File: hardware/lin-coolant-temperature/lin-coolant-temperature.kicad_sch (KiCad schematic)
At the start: 25 parts, among them J1 UPDI, J2 I2C LCD, J3 Screw_Terminal_01x03, Q1 2N7002, Q2 2N7002, U1 TJA1021T, U2 ATtiny824-X, U3 PCA9536DP

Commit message: Add firmware for lin-coolant-temperature, cleanup layout
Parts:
- added D1: LED, LED_SMD:LED_0805_2012Metric_Pad1.15x1.40mm_HandSolder, symbol Device:LED
- added R5: 330, Resistor_SMD:R_0805_2012Metric_Pad1.20x1.40mm_HandSolder, symbol Device:R
- renumbered D1 to D2, R9 to R10, R5 to R6, R6 to R7, R7 to R8, R8 to R9
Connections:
- net GND: now also D1.1 (K)
- net at U2.5 (PA7): now also R5.1
- new net: D1.2 (A), R5.2
- no-connect marks 5 -> 4

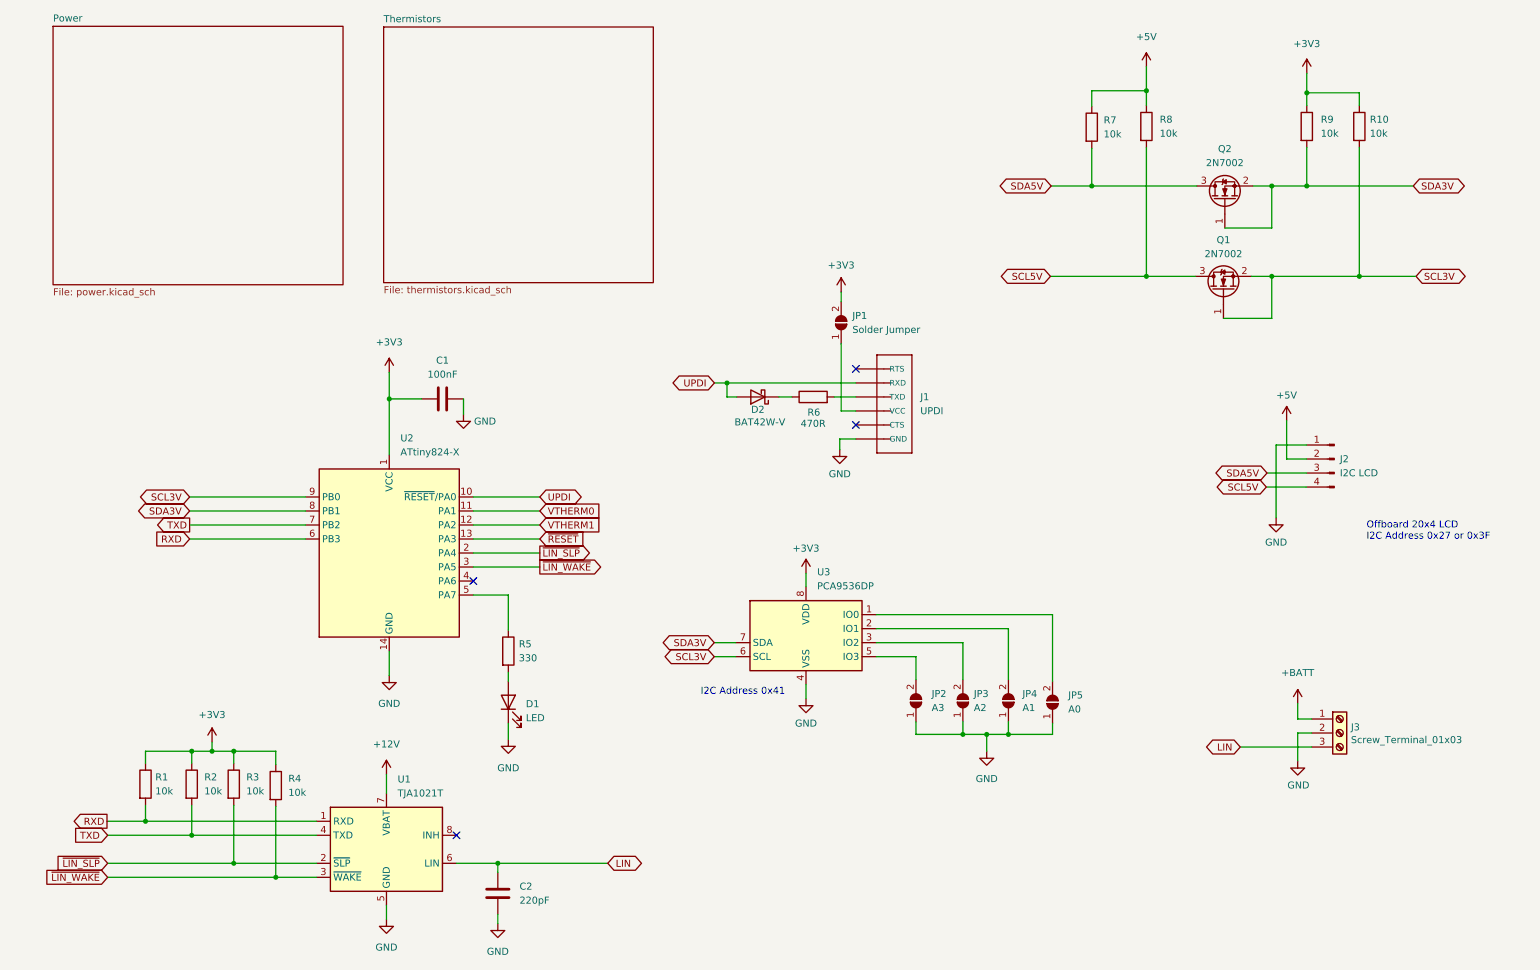
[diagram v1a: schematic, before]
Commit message: Update the schematics... remove PCA9536, use voltage regulator
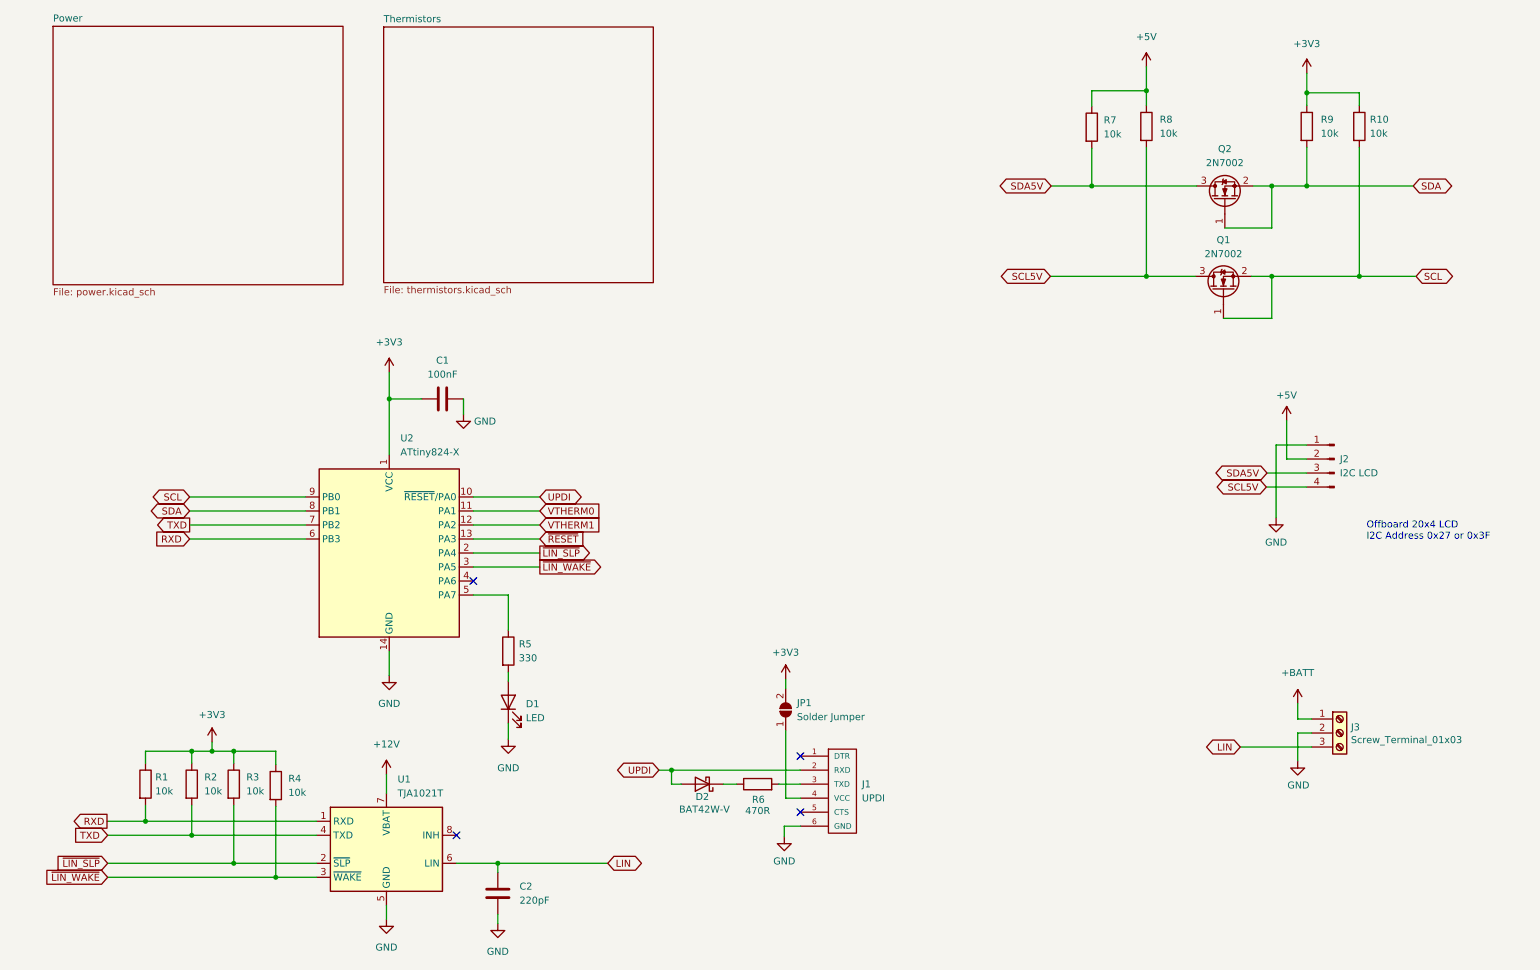
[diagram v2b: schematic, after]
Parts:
- removed JP2: A3, Jumper:SolderJumper-2_P1.3mm_Open_TrianglePad1.0x1.5mm, symbol Jumper:SolderJumper_2_Open
- removed JP3: A2, Jumper:SolderJumper-2_P1.3mm_Open_TrianglePad1.0x1.5mm, symbol Jumper:SolderJumper_2_Open
- removed JP4: A1, Jumper:SolderJumper-2_P1.3mm_Open_TrianglePad1.0x1.5mm, symbol Jumper:SolderJumper_2_Open
- removed JP5: A0, Jumper:SolderJumper-2_P1.3mm_Open_TrianglePad1.0x1.5mm, symbol Jumper:SolderJumper_2_Open
- removed U3: PCA9536DP, Package_SO:TSSOP-8_3x3mm_P0.65mm, symbol Interface_Expansion:PCA9536DP
- J1: footprint Beirdo:FTDI_BASIC -> Beirdo:FTDI-TARGET; symbol Beirdo:FTDI_BASICPTH -> Beirdo:FTDI-TARGET
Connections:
- net GND: now also J1.6 (GND); no longer J1.1 (GND)
- net UPDI: now also J1.2 (RXD); no longer J1.5 (RXD)
- net at J1.3 (TXD): now also R6.2; no longer JP1.1 (A)
- net at J1.4 (VCC): now also JP1.1 (A); no longer R6.2
- net SCL3V renamed SCL
- net SDA3V renamed SDA
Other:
- note removed: "I2C Address 0x41"
- moved on the sheet: D2, JP1, R6
